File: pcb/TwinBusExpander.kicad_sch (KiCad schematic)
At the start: 28 parts, among them J1 USB_C_Receptacle_USB2.0_16P, J2 Twinbus 7630, Q1 AO3400A, SW1 Reset, SW2 Boot, U1 PC817X3C, U2 PC817X3C, U3 AMS1117-3.3, U4 ESP32-C6-WROOM-1

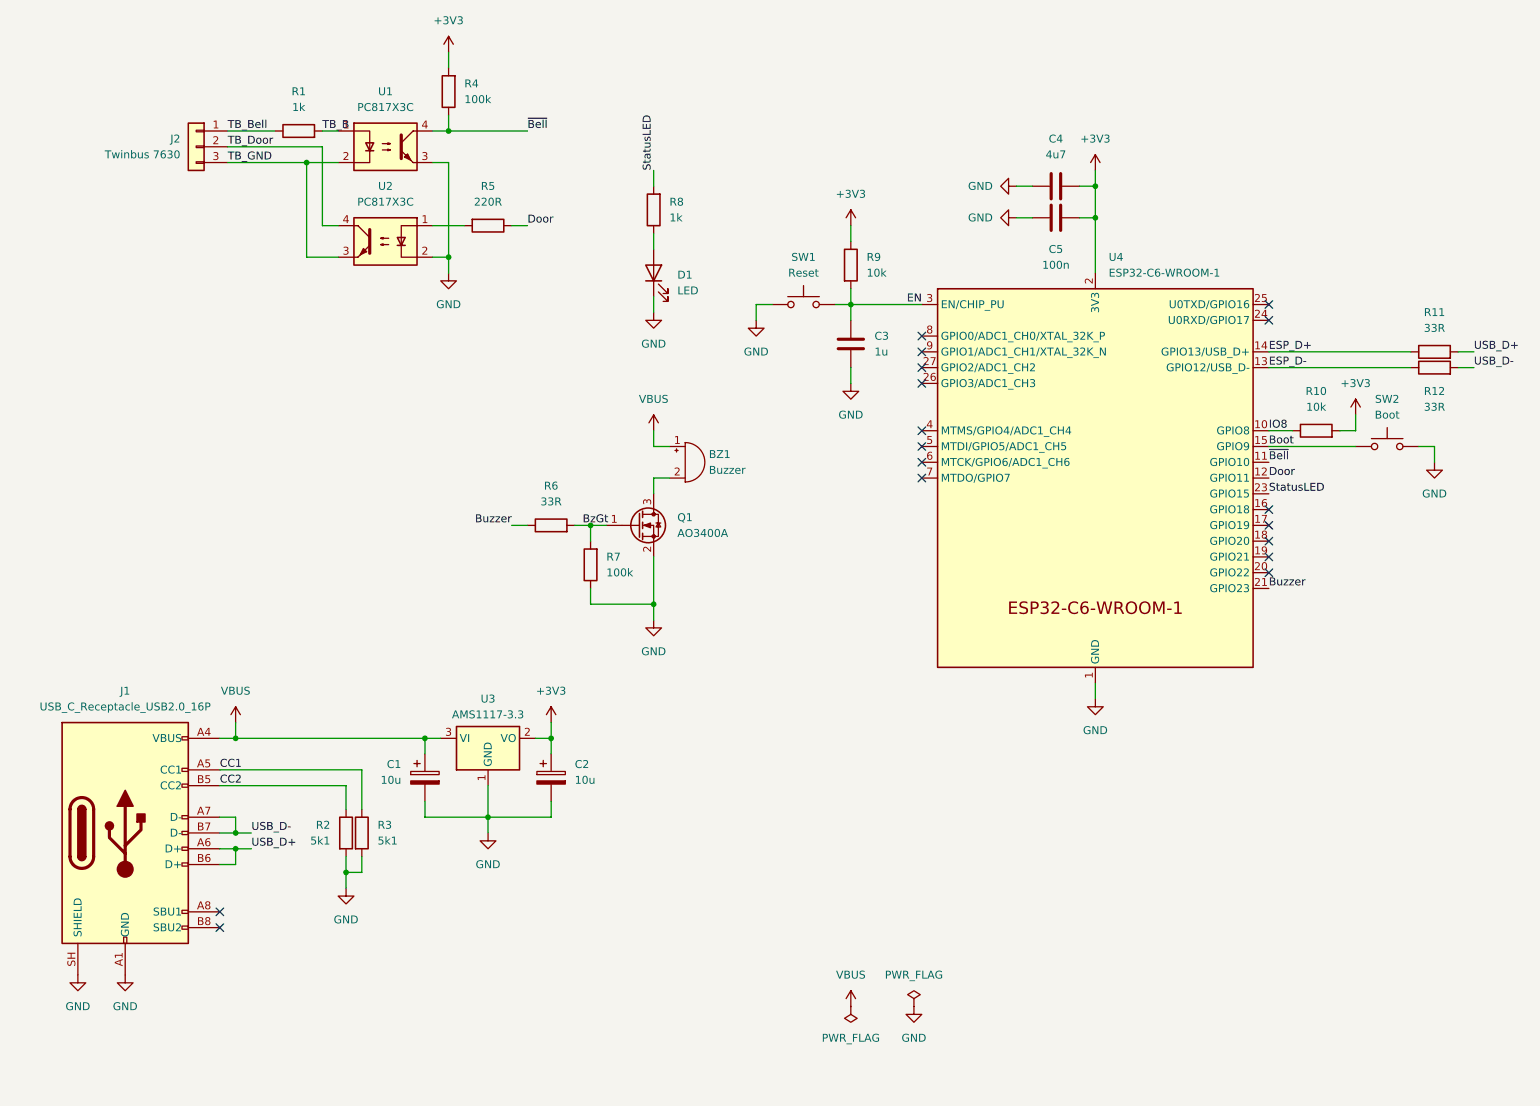
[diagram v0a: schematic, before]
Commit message: feat!: remove speaker completely
Speaker didnt work as planned, removed. Board got a lot smaller.
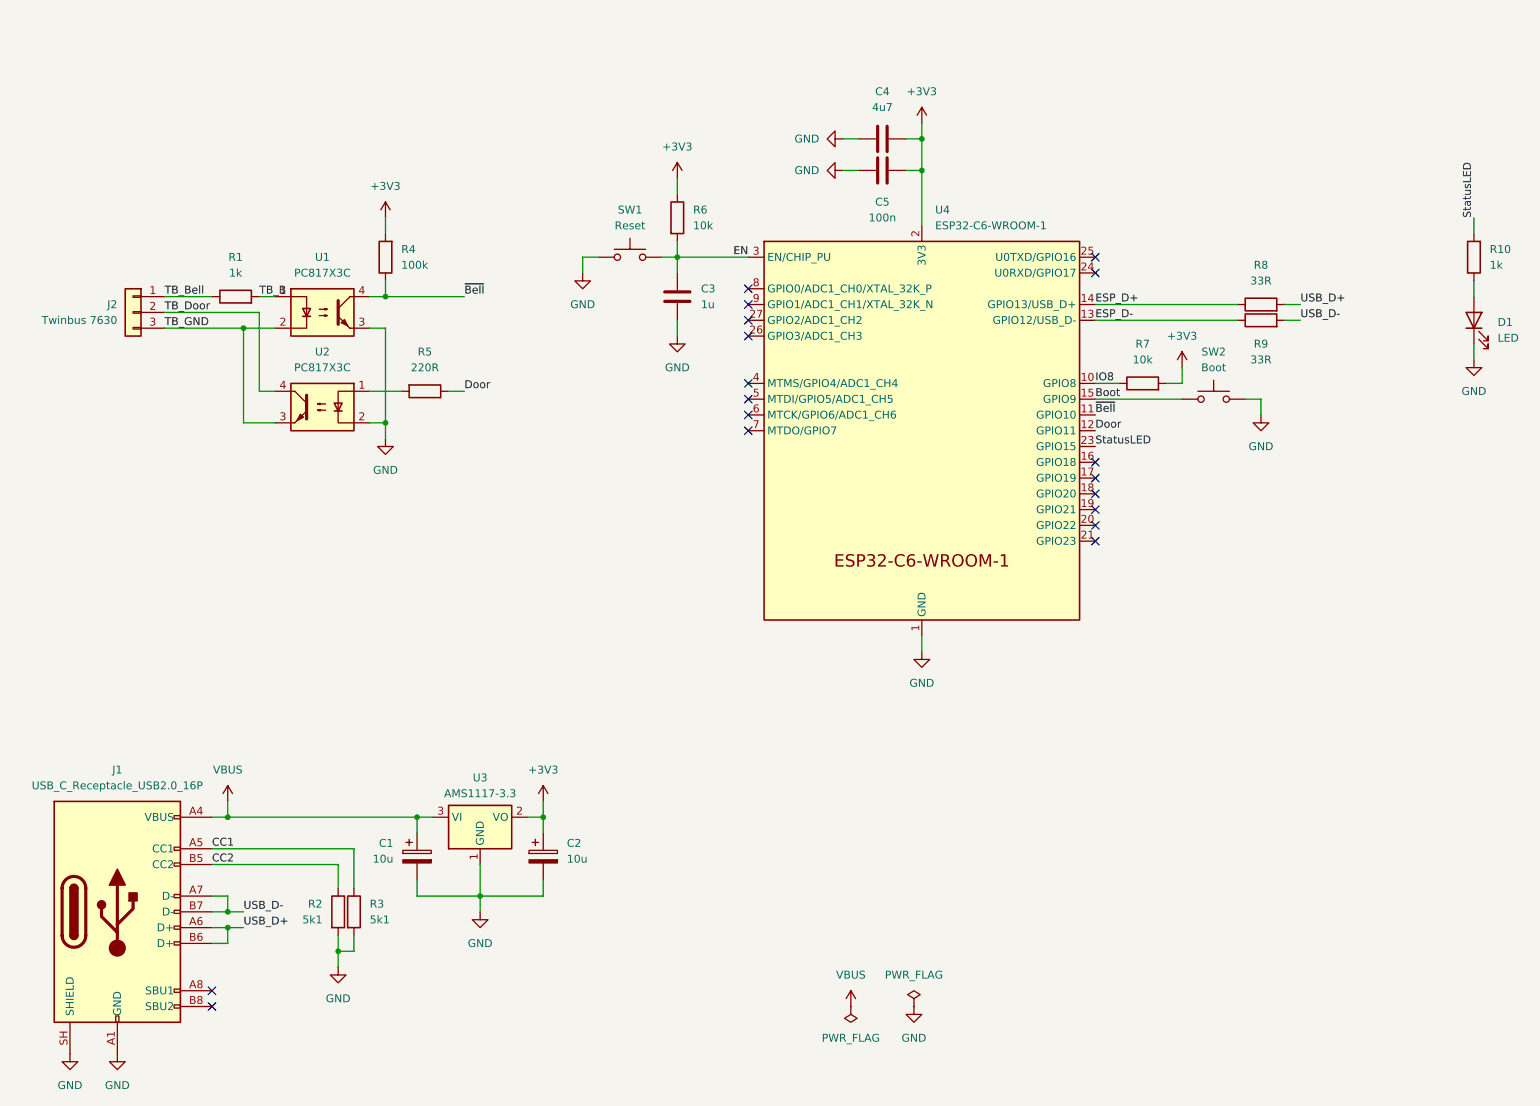
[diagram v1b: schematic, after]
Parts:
- removed BZ1: Buzzer, Buzzer_Beeper:Buzzer_TDK_PS1240P02BT_D12.2mm_H6.5mm, symbol Device:Buzzer
- removed Q1: AO3400A, Package_TO_SOT_SMD:SOT-23, symbol Transistor_FET:AO3400A
- removed R6: 33R, Resistor_SMD:R_0402_1005Metric, symbol Device:R
- removed R7: 100k, Resistor_SMD:R_0402_1005Metric, symbol Device:R
- renumbered R8 to R10, R9 to R6, R10 to R7, R11 to R8, R12 to R9
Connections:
- net Buzzer: no longer names the net of U4.21 (GPIO23)
- no-connect marks 17 -> 18
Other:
- moved on the sheet: C1, C2, C3, C4, C5, D1, J1, J2, R1, R10, R2, R3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

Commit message: feat: replace Optoisolators
Replace generic PC817 with LTV-817S because of part availability
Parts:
- removed U1, U2: PC817X3C, Package_DIP:SMDIP-4_W9.53mm, symbol Isolator:PC817
- added U1, U2: LTV-817S, Package_DIP:SMDIP-4_W9.53mm, symbol Isolator:LTV-817S
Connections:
- net GND: now also U1.3, U2.2
- net TB_B: now also U1.1
- net TB_Door: now also U2.4
- net TB_GND: now also U1.2, U2.3
- net ~{Bell}: now also U1.4
- net at R5.2: now also U2.1
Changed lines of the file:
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@@
 	)
 	(symbol
-		(lib_id "Isolator:PC817")
-		(at 72.39 68.58 0)
-		(unit 1)
-		(body_style 1)
-		(exclude_from_sim no)
-		(in_bom yes)
-		(on_board yes)
-		(in_pos_files yes)
-		(dnp no)
-		(property "Reference" "U1"
-			(at 72.39 59.69 0)
-			(show_name no)
-			(do_not_autoplace no)
-			(effects
-				(font
-					(size 1.27 1.27)
-				)
-			)
-		)
-		(property "Value" "PC817X3C"
-			(at 72.39 62.23 0)
-			(show_name no)
-			(do_not_autoplace no)
-			(effects
-				(font
-					(size 1.27 1.27)
-				)
-			)
-		)
-		(property "Footprint" "Package_DIP:SMDIP-4_W9.53mm"
-			(at 67.31 73.66 0)
-			(hide yes)
-			(show_name no)
-			(do_not_autoplace no)
-			(effects
-				(font
-					(size 1.27 1.27)
-					(italic yes)
-				)
-				(justify left)
-			)
-		)
-		(property "Datasheet" "http://www.soselectronic.cz/a_info/resource/d/pc817.pdf"
-			(at 72.39 68.58 0)
-			(hide yes)
-			(show_name no)
-			(do_not_autoplace no)
-			(effects
-				(font
-					(size 1.27 1.27)
-				)
-				(justify left)
-			)
-		)
-		(property "Description" "DC Optocoupler, Vce 35V, CTR 50-300%, DIP-4"
-			(at 72.39 68.58 0)
-			(hide yes)
-			(show_name no)
-			(do_not_autoplace no)
-			(effects
-				(font
-					(size 1.27 1.27)
-				)
-			)
-		)
-		(property "LCSC" "C41807"
-			(at 72.39 68.58 0)
-			(hide yes)
-			(show_name no)
-			(do_not_autoplace no)
-			(effects
-				(font
-					(size 1.27 1.27)
-				)
-			)
-		)
-		(pin "2"
-		)
-		(pin "3"
-		)
-		(pin "4"
-		)
-		(pin "1"
-		)
-		(instances
-			(project "TwinBusExpander"
-				(path "/df90c09d-6965-4a0b-ae16-1649db1f90b9"
-					(reference "U1")
-					(unit 1)
-				)
-			)
-		)
-	)
-	(symbol
 		(lib_id "power:GND")
 		(at 156.21 40.64 270)
@@
 	)
 	(symbol
+		(lib_id "Isolator:LTV-817S")
+		(at 72.39 83.82 0)
+		(mirror y)
+		(unit 1)
+		(body_style 1)
+		(exclude_from_sim no)
+		(in_bom yes)
+		(on_board yes)
+		(in_pos_files yes)
+		(dnp no)
+		(property "Reference" "U2"
+			(at 72.39 74.93 0)
+			(show_name no)
+			(do_not_autoplace no)
+			(effects
+				(font
+					(size 1.27 1.27)
+				)
+			)
+		)
+		(property "Value" "LTV-817S"
+			(at 72.39 77.47 0)
+			(show_name no)
+			(do_not_autoplace no)
+			(effects
+				(font
+					(size 1.27 1.27)
+				)
+			)
+		)
+		(property "Footprint" "Package_DIP:SMDIP-4_W9.53mm"
+			(at 72.39 91.44 0)
+			(hide yes)
+			(show_name no)
+			(do_not_autoplace no)
+			(effects
+				(font
+					(size 1.27 1.27)
+				)
+			)
+		)
+		(property "Datasheet" "http://www.us.liteon.com/downloads/LTV-817-827-847.PDF"
+			(at 81.28 76.2 0)
+			(hide yes)
+			(show_name no)
+			(do_not_autoplace no)
+			(effects
+				(font
+					(size 1.27 1.27)
+				)
+			)
+		)
+		(property "Description" "DC Optocoupler, Vce 35V, CTR 50%, SMDIP-4"
+			(at 72.39 83.82 0)
+			(hide yes)
+			(show_name no)
+			(do_not_autoplace no)
+			(effects
+				(font
+					(size 1.27 1.27)
+				)
+			)
+		)
+		(property "LCSC" "C109227"
+			(at 72.39 83.82 0)
+			(hide yes)
+			(show_name no)
+			(do_not_autoplace no)
+			(effects
+				(font
+					(size 1.27 1.27)
+				)
+			)
+		)
+		(pin "4"
+		)
+		(pin "1"
+		)
+		(pin "3"
+		)
+		(pin "2"
+		)
+		(instances
+			(project "TwinBusExpander"
+				(path "/df90c09d-6965-4a0b-ae16-1649db1f90b9"
+					(reference "U2")
+					(unit 1)
+				)
+			)
+		)
+	)
+	(symbol
 		(lib_id "Device:R")
 		(at 74.93 165.1 0)
@@
 	)
 	(symbol
+		(lib_id "Isolator:LTV-817S")
+		(at 72.39 68.58 0)
+		(unit 1)
+		(body_style 1)
+		(exclude_from_sim no)
+		(in_bom yes)
+		(on_board yes)
+		(in_pos_files yes)
+		(dnp no)
+		(fields_autoplaced yes)
+		(property "Reference" "U1"
+			(at 72.39 59.69 0)
+			(show_name no)
+			(do_not_autoplace no)
+			(effects
+				(font
+					(size 1.27 1.27)
+				)
+			)
+		)
+		(property "Value" "LTV-817S"
+			(at 72.39 62.23 0)
+			(show_name no)
+			(do_not_autoplace no)
+			(effects
+				(font
+					(size 1.27 1.27)
+				)
+			)
+		)
+		(property "Footprint" "Package_DIP:SMDIP-4_W9.53mm"
+			(at 72.39 76.2 0)
+			(hide yes)
+			(show_name no)
+			(do_not_autoplace no)
+			(effects
+				(font
+					(size 1.27 1.27)
+				)
+			)
+		)
+		(property "Datasheet" "http://www.us.liteon.com/downloads/LTV-817-827-847.PDF"
+			(at 63.5 60.96 0)
+			(hide yes)
+			(show_name no)
+			(do_not_autoplace no)
+			(effects
+				(font
+					(size 1.27 1.27)
+				)
+			)
+		)
+		(property "Description" "DC Optocoupler, Vce 35V, CTR 50%, SMDIP-4"
+			(at 72.39 68.58 0)
+			(hide yes)
+			(show_name no)
+			(do_not_autoplace no)
+			(effects
+				(font
+					(size 1.27 1.27)
+				)
+			)
+		)
+		(property "LCSC" "C109227"
+			(at 72.39 68.58 0)
+			(hide yes)
+			(show_name no)
+			(do_not_autoplace no)
+			(effects
+				(font
+					(size 1.27 1.27)
+				)
+			)
+		)
+		(pin "4"
+		)
+		(pin "1"
+		)
+		(pin "3"
+		)
+		(pin "2"
+		)
+		(instances
+			(project "TwinBusExpander"
+				(path "/df90c09d-6965-4a0b-ae16-1649db1f90b9"
+					(reference "U1")
+					(unit 1)
+				)
+			)
+		)
+	)
+	(symbol
 		(lib_id "Device:R")
 		(at 58.42 66.04 90)
@@
 					(unit 1)
 				)
-			)
-		)
-	)
-	(symbol
-		(lib_id "Isolator:PC817")
-		(at 72.39 83.82 0)
-		(mirror y)
-		(unit 1)
-		(body_style 1)
-		(exclude_from_sim no)
-		(in_bom yes)
-		(on_board yes)
-		(in_pos_files yes)
-		(dnp no)
-		(property "Reference" "U2"
-			(at 72.39 74.93 0)
-			(show_name no)
-			(do_not_autoplace no)
-			(effects
-				(font
-					(size 1.27 1.27)
-				)
-			)
-		)
-		(property "Value" "PC817X3C"
-			(at 72.39 77.47 0)
-			(show_name no)
-			(do_not_autoplace no)
-			(effects
-				(font
-					(size 1.27 1.27)
-				)
-			)
-		)
-		(property "Footprint" "Package_DIP:SMDIP-4_W9.53mm"
-			(at 77.47 88.9 0)
-			(hide yes)
-			(show_name no)
-			(do_not_autoplace no)
-			(effects
-				(font
-					(size 1.27 1.27)
-					(italic yes)
-				)
-				(justify left)
-			)
-		)
-		(property "Datasheet" "http://www.soselectronic.cz/a_info/resource/d/pc817.pdf"
-			(at 72.39 83.82 0)
-			(hide yes)
-			(show_name no)
-			(do_not_autoplace no)
-			(effects
-				(font
-					(size 1.27 1.27)
-				)
-				(justify left)
-			)
-		)
-		(property "Description" "DC Optocoupler, Vce 35V, CTR 50-300%, DIP-4"
-			(at 72.39 83.82 0)
-			(hide yes)
-			(show_name no)
-			(do_not_autoplace no)
-			(effects
-				(font
-					(size 1.27 1.27)
-				)
-			)
-		)
-		(property "LCSC" "C41807"
-			(at 72.39 83.82 0)
-			(hide yes)
-			(show_name no)
-			(do_not_autoplace no)
-			(effects
-				(font
-					(size 1.27 1.27)
-				)
-			)
-		)
-		(pin "2"
-		)
-		(pin "3"
-		)
-		(pin "4"
-		)
-		(pin "1"
-		)
-		(instances
-			(project "TwinBusExpander"
-				(path "/df90c09d-6965-4a0b-ae16-1649db1f90b9"
-					(reference "U2")
-					(unit 1)
-				)
